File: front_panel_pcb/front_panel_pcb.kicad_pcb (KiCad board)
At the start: 2 copper layers, 93.3 x 100 mm, 42 parts

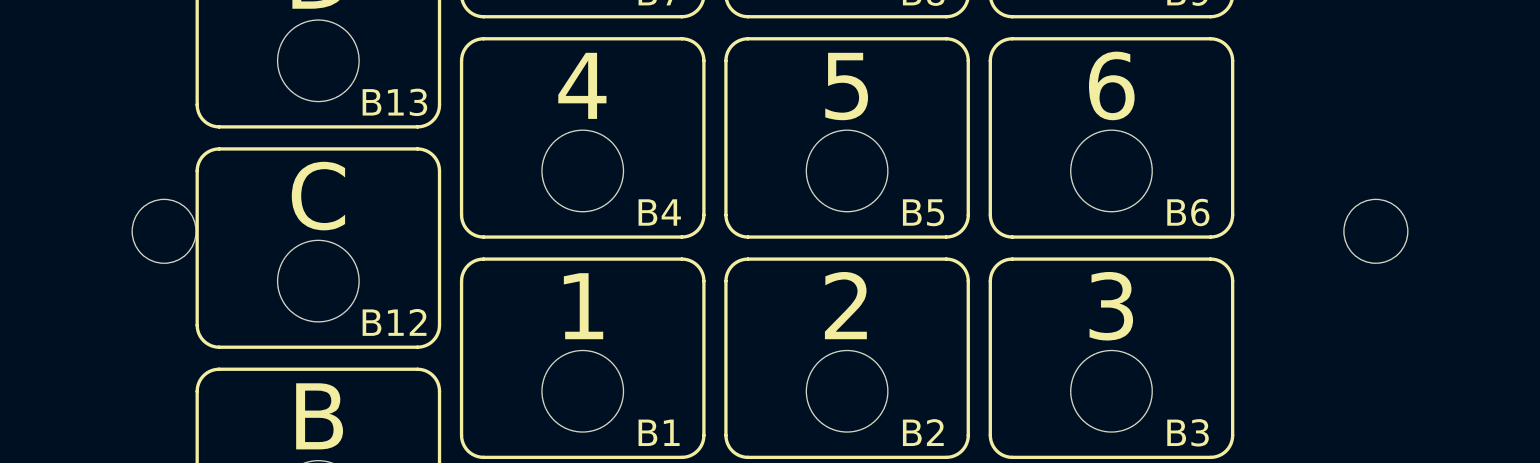
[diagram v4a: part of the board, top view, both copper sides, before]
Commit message: remove battery, there will be no screws on front panel
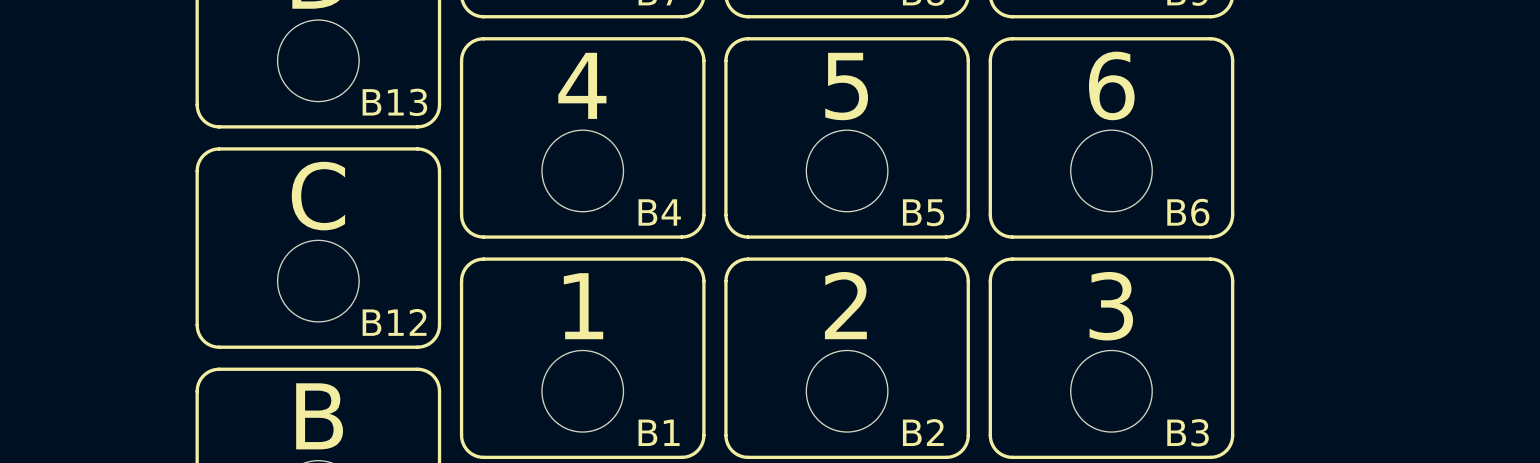
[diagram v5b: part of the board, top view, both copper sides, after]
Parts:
- removed BT1: 4 Cell AA Battery Clip, MPD:BC4AAW
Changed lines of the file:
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@@
     (tracks 0)
     (zones 0)
-    (modules 42)
+    (modules 41)
     (nets 1)
   )
@@
     (uvia_drill 0.4)
   )
-  (module MPD:BC4AAW (layer B.Cu)
-    (at 102.5 114.57 90)
-    (fp_text reference BT1 (at 0 0.75 90) (layer B.SilkS)
-      (effects (font (size 1 1) (thickness 0.15)) (justify mirror))
-    )
-    (fp_text value "4 Cell AA Battery Clip" (at 0 -4 90) (layer B.Fab)
-      (effects (font (size 1 1) (thickness 0.15)) (justify mirror))
-    )
-    (fp_circle (center 0 -27.5) (end 3.6 -27.5) (layer F.Fab) (width 0.15))
-    (fp_circle (center 0 27.5) (end 3.6 27.6) (layer F.Fab) (width 0.15))
-    (fp_line (start -28.5 30.4) (end 28.5 30.4) (layer B.SilkS) (width 0.15))
-    (fp_line (start -28.5 -30.7) (end -28.5 30.4) (layer B.SilkS) (width 0.15))
-    (fp_line (start 28.5 -30.7) (end -28.5 -30.7) (layer B.SilkS) (width 0.15))
-    (fp_line (start 28.5 30.4) (end 28.5 -30.7) (layer B.SilkS) (width 0.15))
-    (fp_text user "BC4AAPC 4 AA Battery Holder" (at 0 -0.75 90) (layer B.SilkS)
-      (effects (font (size 1 1) (thickness 0.15)) (justify mirror))
-    )
-    (fp_line (start 21 3) (end 20 3) (layer B.SilkS) (width 0.15))
-    (fp_line (start 21 10) (end 21 3) (layer B.SilkS) (width 0.15))
-    (fp_line (start 20 10) (end 21 10) (layer B.SilkS) (width 0.15))
-    (fp_line (start -21 17) (end -20 17) (layer B.SilkS) (width 0.15))
-    (fp_line (start -21 23) (end -21 17) (layer B.SilkS) (width 0.15))
-    (fp_line (start -20 23) (end -21 23) (layer B.SilkS) (width 0.15))
-    (fp_line (start -21 -10) (end -20 -10) (layer B.SilkS) (width 0.15))
-    (fp_line (start -21 -4) (end -21 -10) (layer B.SilkS) (width 0.15))
-    (fp_line (start -20 -4) (end -21 -4) (layer B.SilkS) (width 0.15))
-    (fp_line (start 21 -23) (end 20 -23) (layer B.SilkS) (width 0.15))
-    (fp_line (start 21 -17) (end 21 -23) (layer B.SilkS) (width 0.15))
-    (fp_line (start 20 -17) (end 21 -17) (layer B.SilkS) (width 0.15))
-    (fp_text user "1.5V AA (LR6)" (at 0 -20 90) (layer B.SilkS)
-      (effects (font (size 1 1) (thickness 0.15)) (justify mirror))
-    )
-    (fp_line (start -21 -10) (end -20 -10) (layer B.Fab) (width 0.15))
-    (fp_line (start -21 -4) (end -21 -10) (layer B.Fab) (width 0.15))
-    (fp_line (start -20 -4) (end -21 -4) (layer B.Fab) (width 0.15))
-    (fp_line (start -21 17) (end -20 17) (layer B.Fab) (width 0.15))
-    (fp_line (start -21 23) (end -21 17) (layer B.Fab) (width 0.15))
-    (fp_line (start -20 23) (end -21 23) (layer B.Fab) (width 0.15))
-    (fp_line (start 21 10) (end 20 10) (layer B.Fab) (width 0.15))
-    (fp_line (start 21 3) (end 21 10) (layer B.Fab) (width 0.15))
-    (fp_line (start 20 3) (end 21 3) (layer B.Fab) (width 0.15))
-    (fp_line (start 21 -23) (end 20 -23) (layer B.Fab) (width 0.15))
-    (fp_line (start 21 -17) (end 21 -23) (layer B.Fab) (width 0.15))
-    (fp_line (start 20 -17) (end 21 -17) (layer B.Fab) (width 0.15))
-    (fp_line (start -20 -15) (end 20 -15) (layer B.Fab) (width 0.15))
-    (fp_line (start -20 -25) (end -20 -15) (layer B.Fab) (width 0.15))
-    (fp_line (start 20 -25) (end -20 -25) (layer B.Fab) (width 0.15))
-    (fp_line (start 20 -15) (end 20 -25) (layer B.Fab) (width 0.15))
-    (fp_line (start -28.6 -30.8) (end -28.6 30.5) (layer B.CrtYd) (width 0.15))
-    (fp_line (start 28.6 -30.8) (end -28.6 -30.8) (layer B.CrtYd) (width 0.15))
-    (fp_line (start 28.6 30.5) (end 28.6 -30.8) (layer B.CrtYd) (width 0.15))
-    (fp_line (start -28.6 30.5) (end 28.6 30.5) (layer B.CrtYd) (width 0.15))
-    (fp_line (start 20 -1.7) (end 20 -11.7) (layer B.Fab) (width 0.15))
-    (fp_line (start 20 11.6) (end 20 1.6) (layer B.Fab) (width 0.15))
-    (fp_line (start 20 24.9) (end 20 14.9) (layer B.Fab) (width 0.15))
-    (fp_line (start -20 -1.7) (end 20 -1.7) (layer B.Fab) (width 0.15))
-    (fp_line (start -20 11.6) (end 20 11.6) (layer B.Fab) (width 0.15))
-    (fp_line (start -20 24.9) (end 20 24.9) (layer B.Fab) (width 0.15))
-    (fp_line (start -20 -11.7) (end -20 -1.7) (layer B.Fab) (width 0.15))
-    (fp_line (start -20 1.6) (end -20 11.6) (layer B.Fab) (width 0.15))
-    (fp_line (start -20 14.9) (end -20 24.9) (layer B.Fab) (width 0.15))
-    (fp_line (start 20 -11.7) (end -20 -11.7) (layer B.Fab) (width 0.15))
-    (fp_line (start 20 1.6) (end -20 1.6) (layer B.Fab) (width 0.15))
-    (fp_line (start 20 14.9) (end -20 14.9) (layer B.Fab) (width 0.15))
-    (fp_line (start -20 -15) (end 20 -15) (layer B.SilkS) (width 0.15))
-    (fp_line (start 20 -25) (end -20 -25) (layer B.SilkS) (width 0.15))
-    (fp_line (start 20 -15) (end 20 -25) (layer B.SilkS) (width 0.15))
-    (fp_line (start -20 -25) (end -20 -15) (layer B.SilkS) (width 0.15))
-    (fp_line (start -20 -11.7) (end -20 -1.7) (layer B.SilkS) (width 0.15))
-    (fp_line (start -20 1.6) (end -20 11.6) (layer B.SilkS) (width 0.15))
-    (fp_line (start -20 14.9) (end -20 24.9) (layer B.SilkS) (width 0.15))
-    (fp_text user "1.5V AA (LR6)" (at 0 -6.7 90) (layer B.SilkS)
-      (effects (font (size 1 1) (thickness 0.15)) (justify mirror))
-    )
-    (fp_text user "1.5V AA (LR6)" (at 0 6.6 90) (layer B.SilkS)
-      (effects (font (size 1 1) (thickness 0.15)) (justify mirror))
-    )
-    (fp_text user "1.5V AA (LR6)" (at 0 19.9 90) (layer B.SilkS)
-      (effects (font (size 1 1) (thickness 0.15)) (justify mirror))
-    )
-    (fp_line (start -20 -1.7) (end 20 -1.7) (layer B.SilkS) (width 0.15))
-    (fp_line (start -20 11.6) (end 20 11.6) (layer B.SilkS) (width 0.15))
-    (fp_line (start -20 24.9) (end 20 24.9) (layer B.SilkS) (width 0.15))
-    (fp_line (start 20 -11.7) (end -20 -11.7) (layer B.SilkS) (width 0.15))
-    (fp_line (start 20 1.6) (end -20 1.6) (layer B.SilkS) (width 0.15))
-    (fp_line (start 20 14.9) (end -20 14.9) (layer B.SilkS) (width 0.15))
-    (fp_line (start 20 -1.7) (end 20 -11.7) (layer B.SilkS) (width 0.15))
-    (fp_line (start 20 11.6) (end 20 1.6) (layer B.SilkS) (width 0.15))
-    (fp_line (start 20 24.9) (end 20 14.9) (layer B.SilkS) (width 0.15))
-    (pad "" np_thru_hole circle (at 0 -27.5 90) (size 2.9 2.9) (drill 2.9) (layers *.Cu *.Mask))
-    (pad "" np_thru_hole circle (at 0 27.5 90) (size 2.9 2.9) (drill 2.9) (layers *.Cu *.Mask))
-    (model ${KIPRJMOD}/3d_models/Battery_MPD.3dshapes/BatteryHolder_BC4AAW001.wrl
-      (at (xyz 0 0 0))
-      (scale (xyz 1 1 1))
-      (rotate (xyz 0 0 0))
-    )
-  )
   (module CK_FP:CK_PTS645_FrontPanel (layer F.Cu)

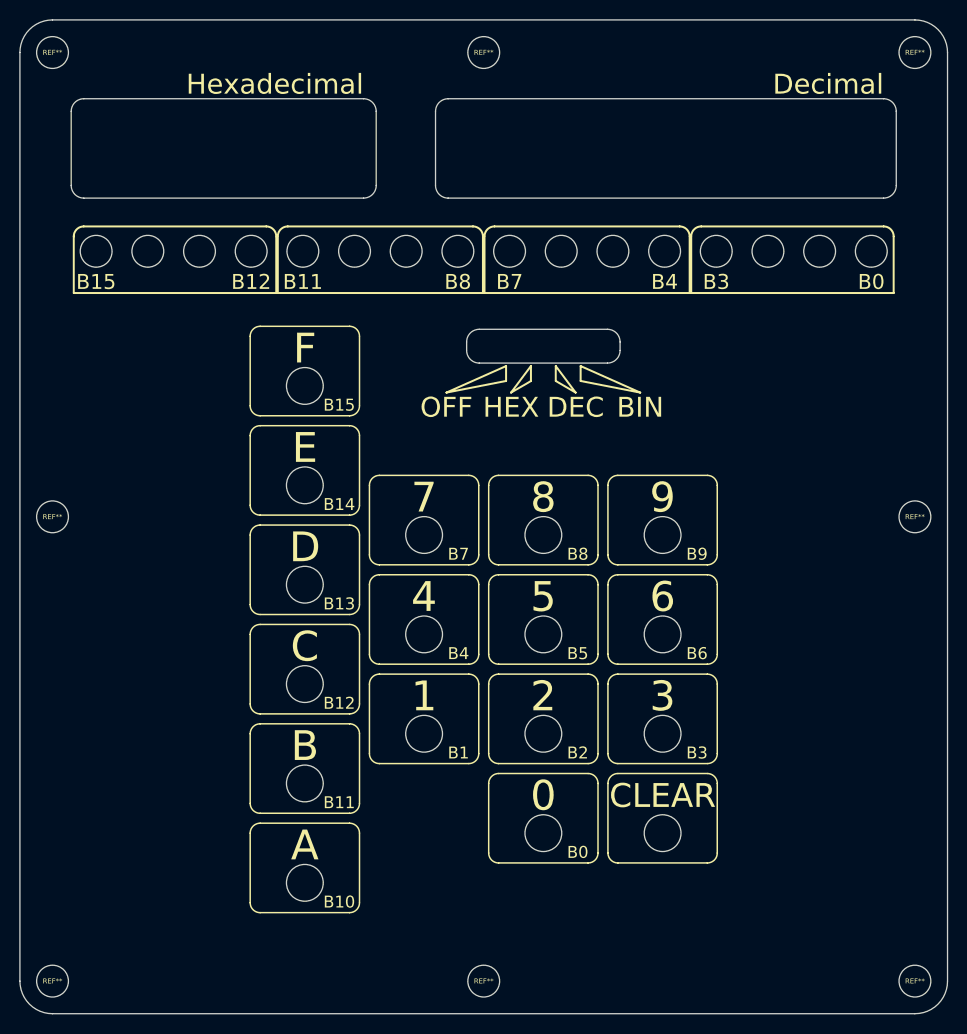
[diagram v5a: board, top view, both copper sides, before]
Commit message: update mounting holes footprints for standoffs
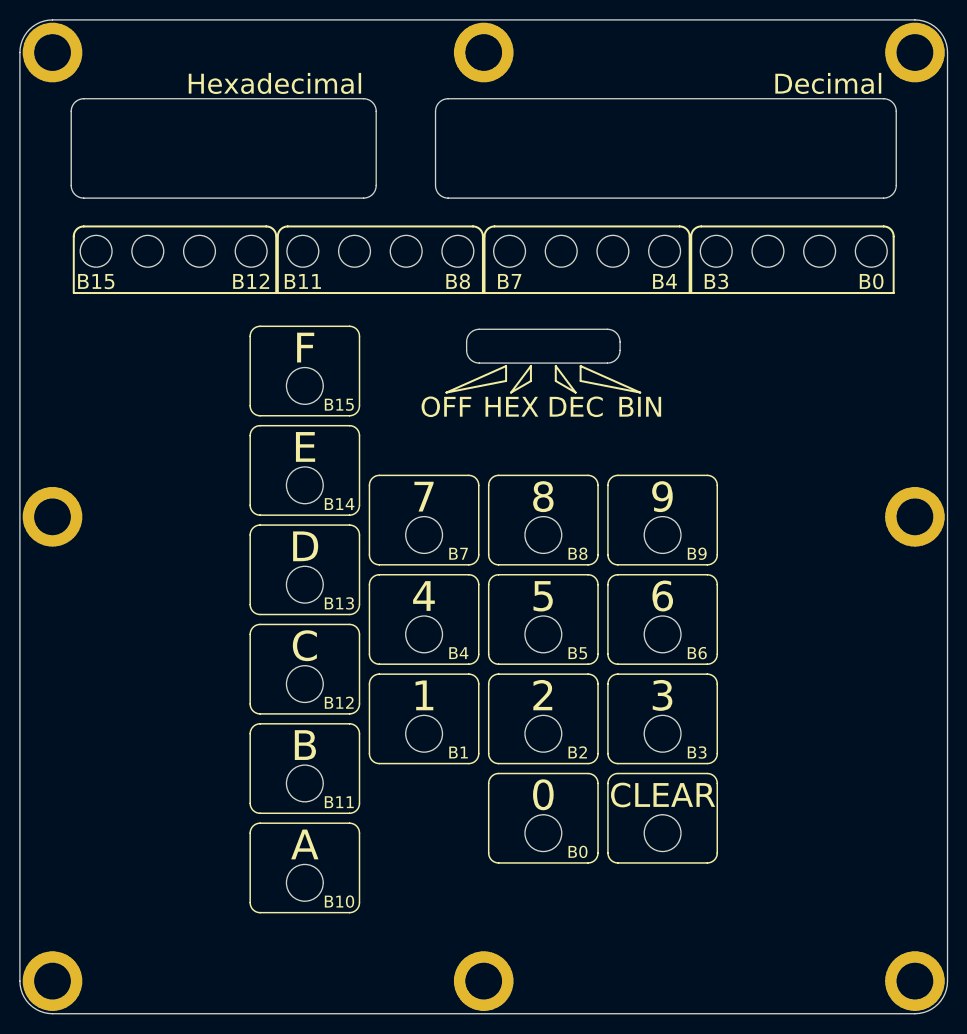
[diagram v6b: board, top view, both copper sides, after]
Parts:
- REF** (x8): footprint Mounting_Holes:MountingHole_3.2mm_M3 -> WE_spacer:WE_RoundSpacer_Unthread_2-5mm_SMD; moved to B.Cu
